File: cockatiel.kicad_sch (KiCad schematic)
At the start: 28 parts

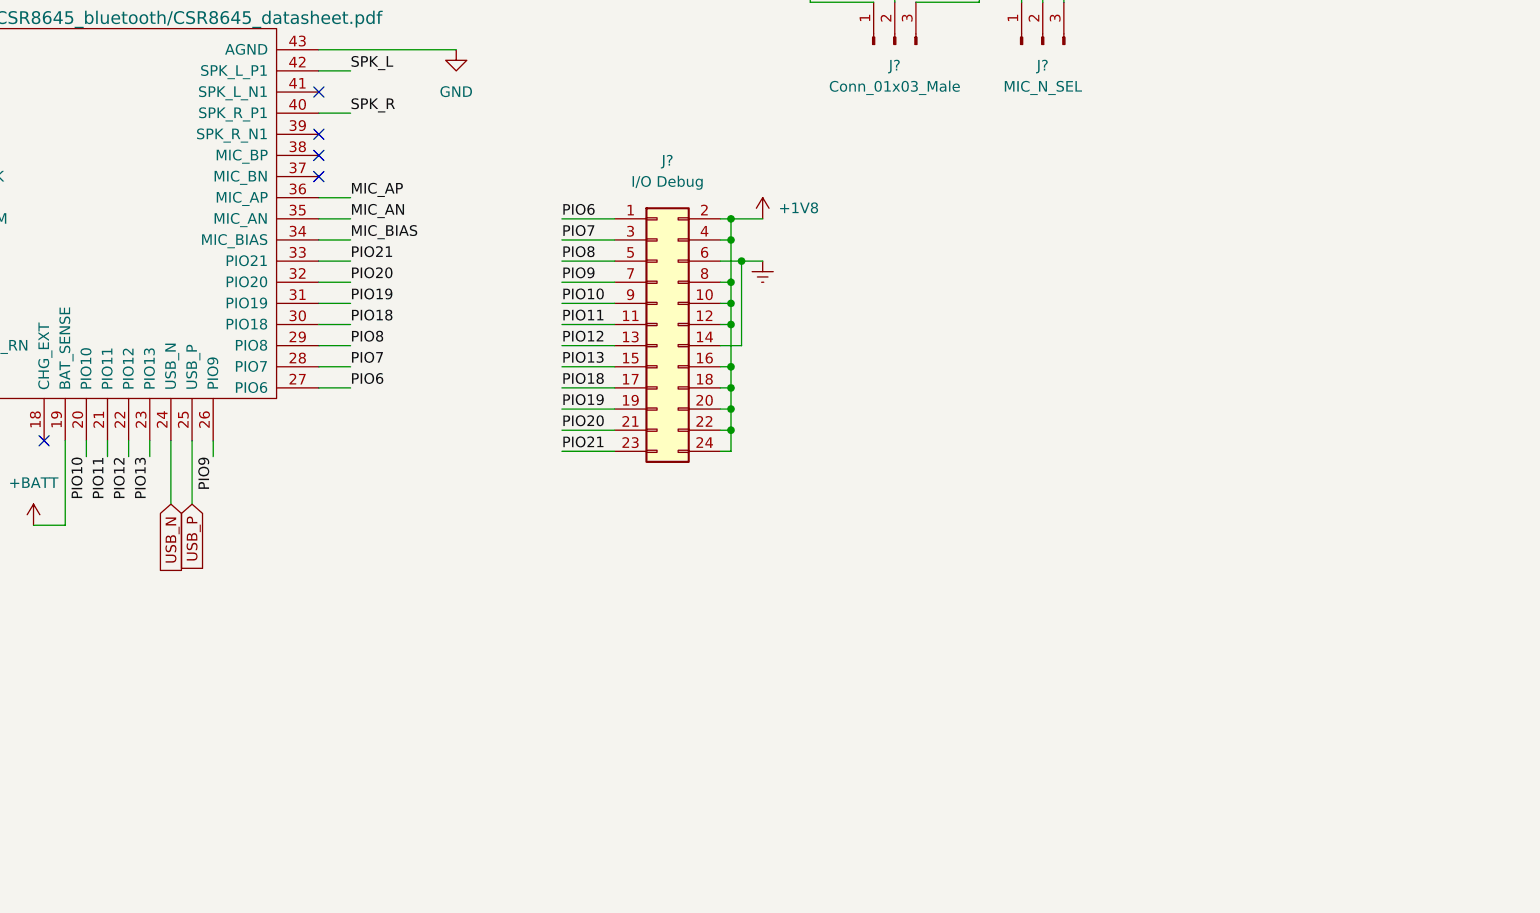
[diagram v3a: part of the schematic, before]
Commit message: Add optional EEPROM
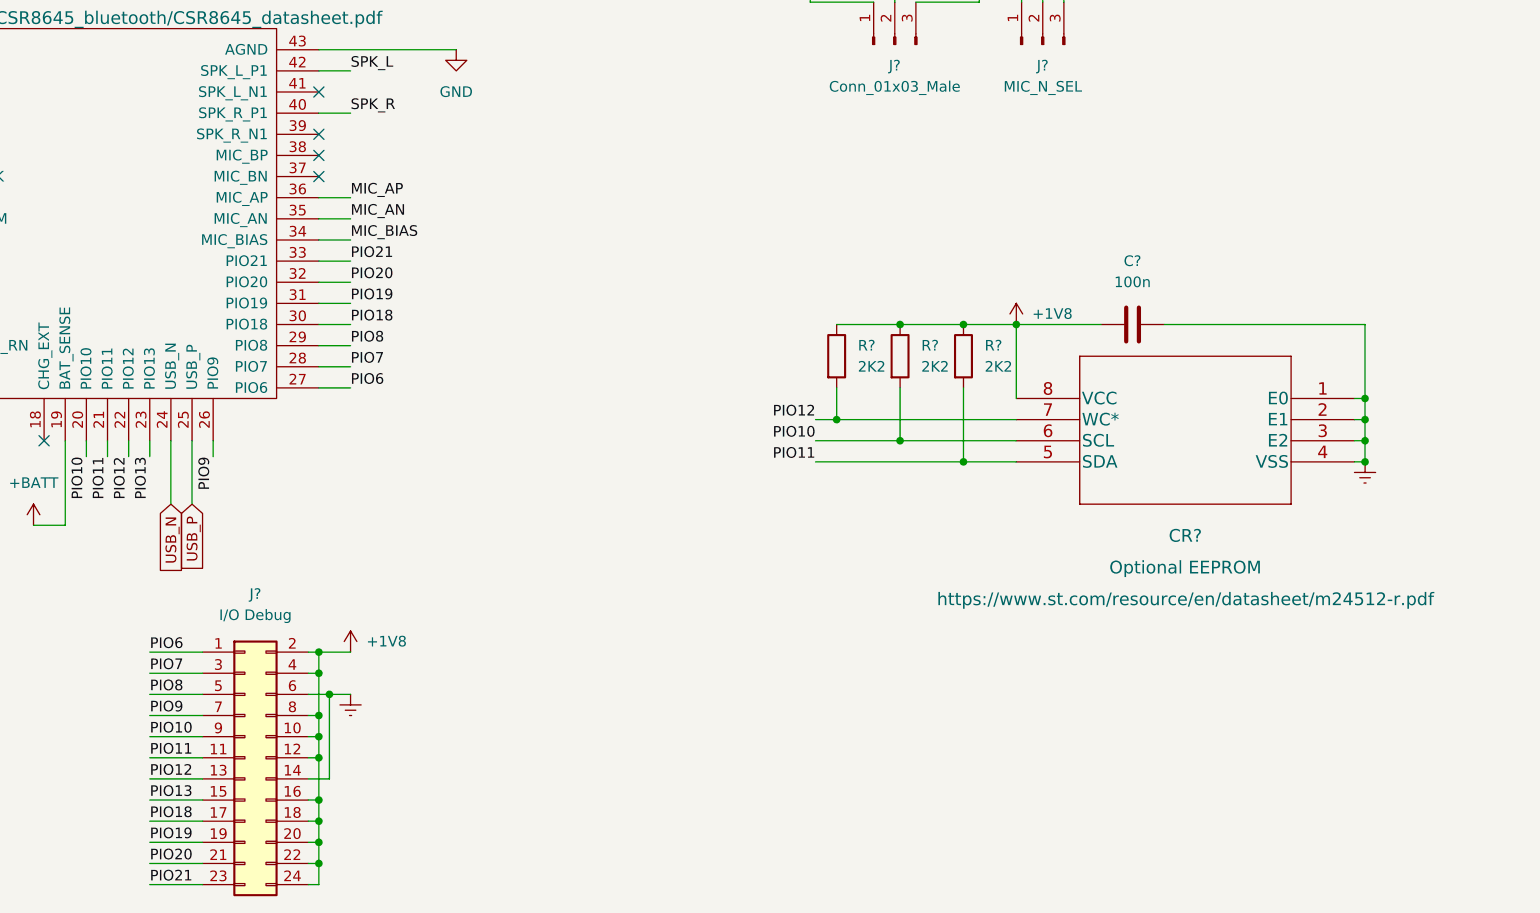
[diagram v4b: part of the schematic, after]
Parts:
- added C?: 100n, Capacitor_SMD:C_0805_2012Metric_Pad1.18x1.45mm_HandSolder, symbol Device:C
- added CR?: Optional EEPROM, st:M24512-RMN6P, symbol 2022-08-27_17-15-02:M24512-RMN6P
- added R? (x3): 2K2, symbol Device:R
- J?: footprint (none) -> Connector_PinHeader_2.54mm:PinHeader_1x04_P2.54mm_Vertical
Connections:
- net +1V8: now also C?.1, CR?.8 (VCC), R?.1, R?.1, R?.1
- net Earth: now also C?.2, CR?.1 (E0), CR?.2 (E1), CR?.3 (E2), CR?.4 (VSS)
- net PIO10: now also CR?.6 (SCL), R?.2
- net PIO11: now also CR?.5 (SDA), R?.2
- net PIO12: now also CR?.7 (WC*), R?.2
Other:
- moved on the sheet: J?

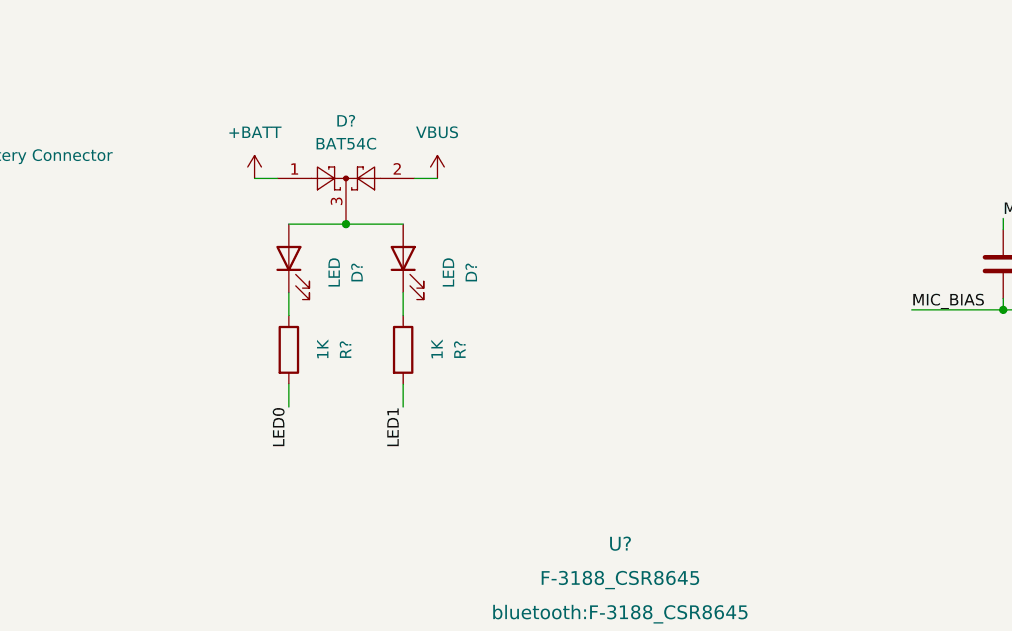
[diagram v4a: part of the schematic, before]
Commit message: Add support for external (panel mount) LEDs
Also correct resistor values to support a set of RGB LEDs.
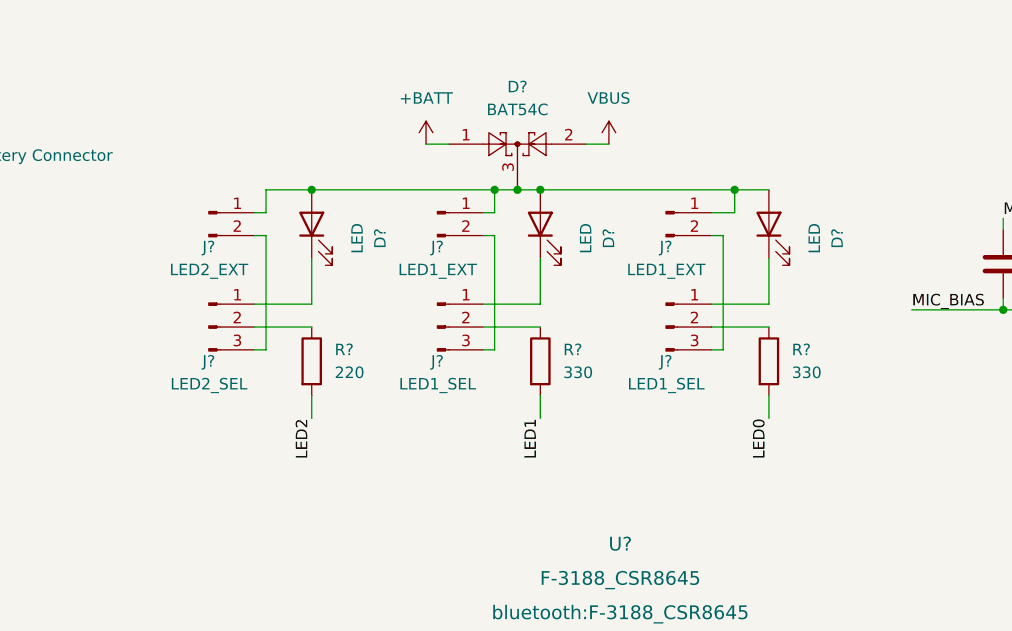
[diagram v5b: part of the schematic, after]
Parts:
- added D?: LED, LED_SMD:LED_0805_2012Metric_Pad1.15x1.40mm_HandSolder, symbol Device:LED
- added J? (x2): LED1_SEL, Connector_PinHeader_2.54mm:PinHeader_1x03_P2.54mm_Vertical, symbol Connector:Conn_01x03_Male
- added J?: LED2_EXT, symbol Connector:Conn_01x02_Male
- added J? (x2): LED1_EXT, Connector_PinHeader_2.54mm:PinHeader_1x02_P2.54mm_Vertical, symbol Connector:Conn_01x02_Male
- added J?: LED2_SEL, Connector_PinHeader_2.54mm:PinHeader_1x03_P2.54mm_Vertical, symbol Connector:Conn_01x03_Male
- added R?: 220, Resistor_SMD:R_0805_2012Metric_Pad1.20x1.40mm_HandSolder, symbol Device:R
- R? (x2): value 1K -> 330
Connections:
- net LED2: now also R?.2
- net at D?.2 (A), D?.2 (A), D?.3: now also D?.2 (A), J?.1 (Pin_1), J?.1 (Pin_1), J?.1 (Pin_1)
- net at D?.1 (K): now also J?.1 (Pin_1); no longer R?.1 (x2)
- new net: J?.2 (Pin_2), R?.1 (x3)
- new net: J?.2 (Pin_2), J?.3 (Pin_3) (x3)
- new net: D?.1 (K), J?.1 (Pin_1)
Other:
- moved on the sheet: D?, R?

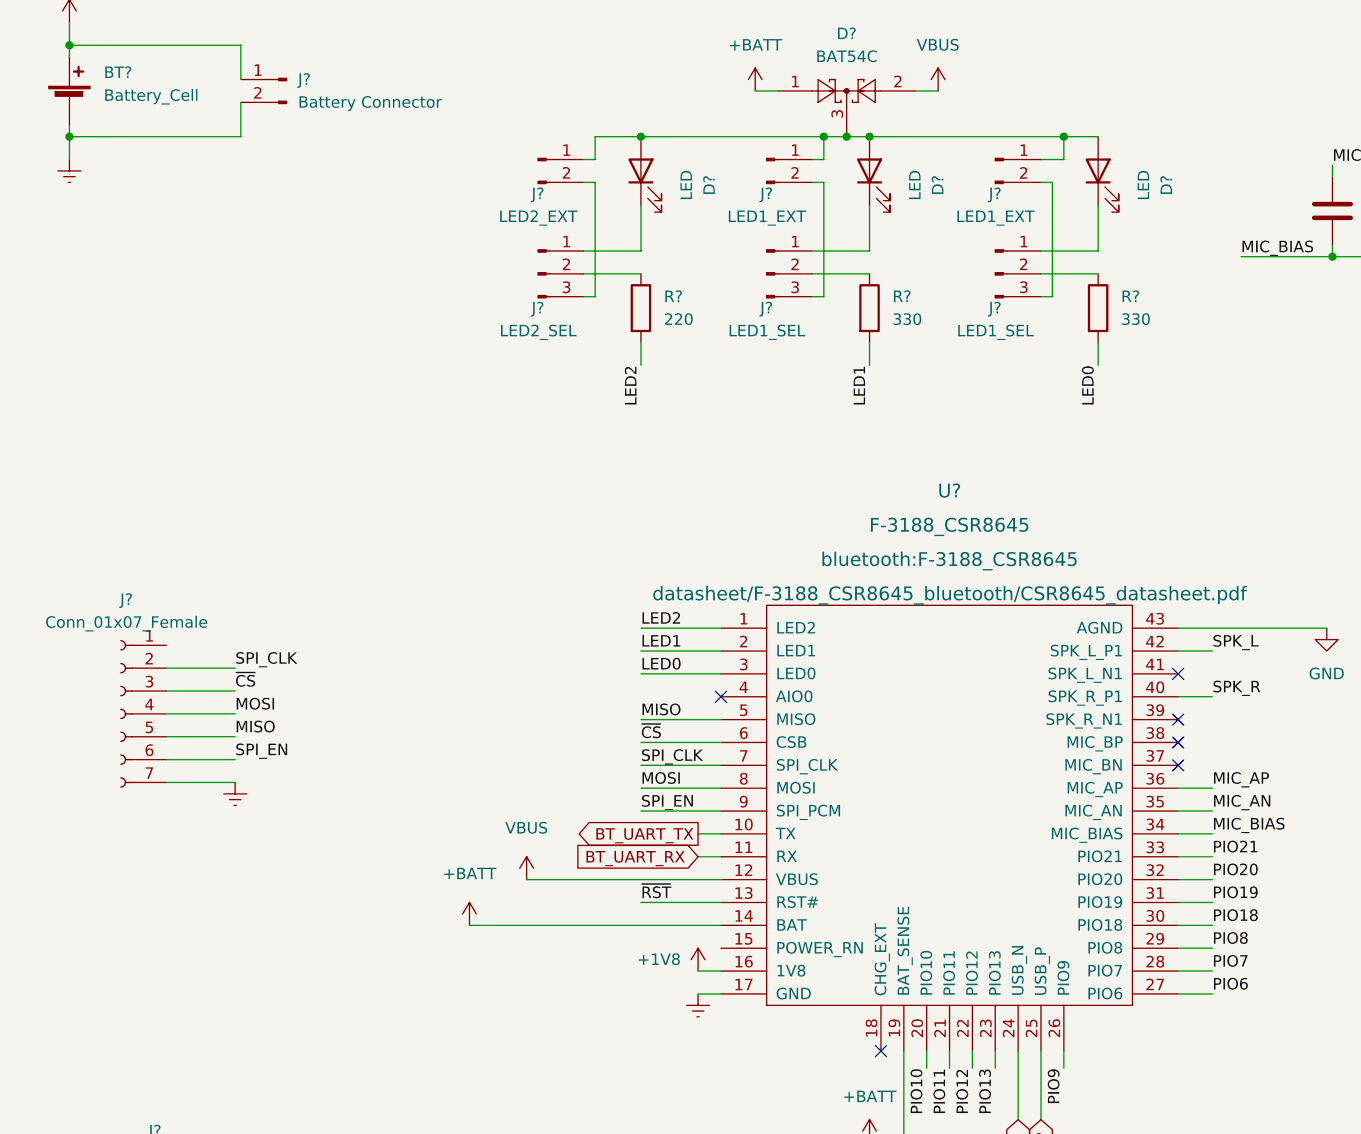
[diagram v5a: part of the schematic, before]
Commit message: Add support for power enable.
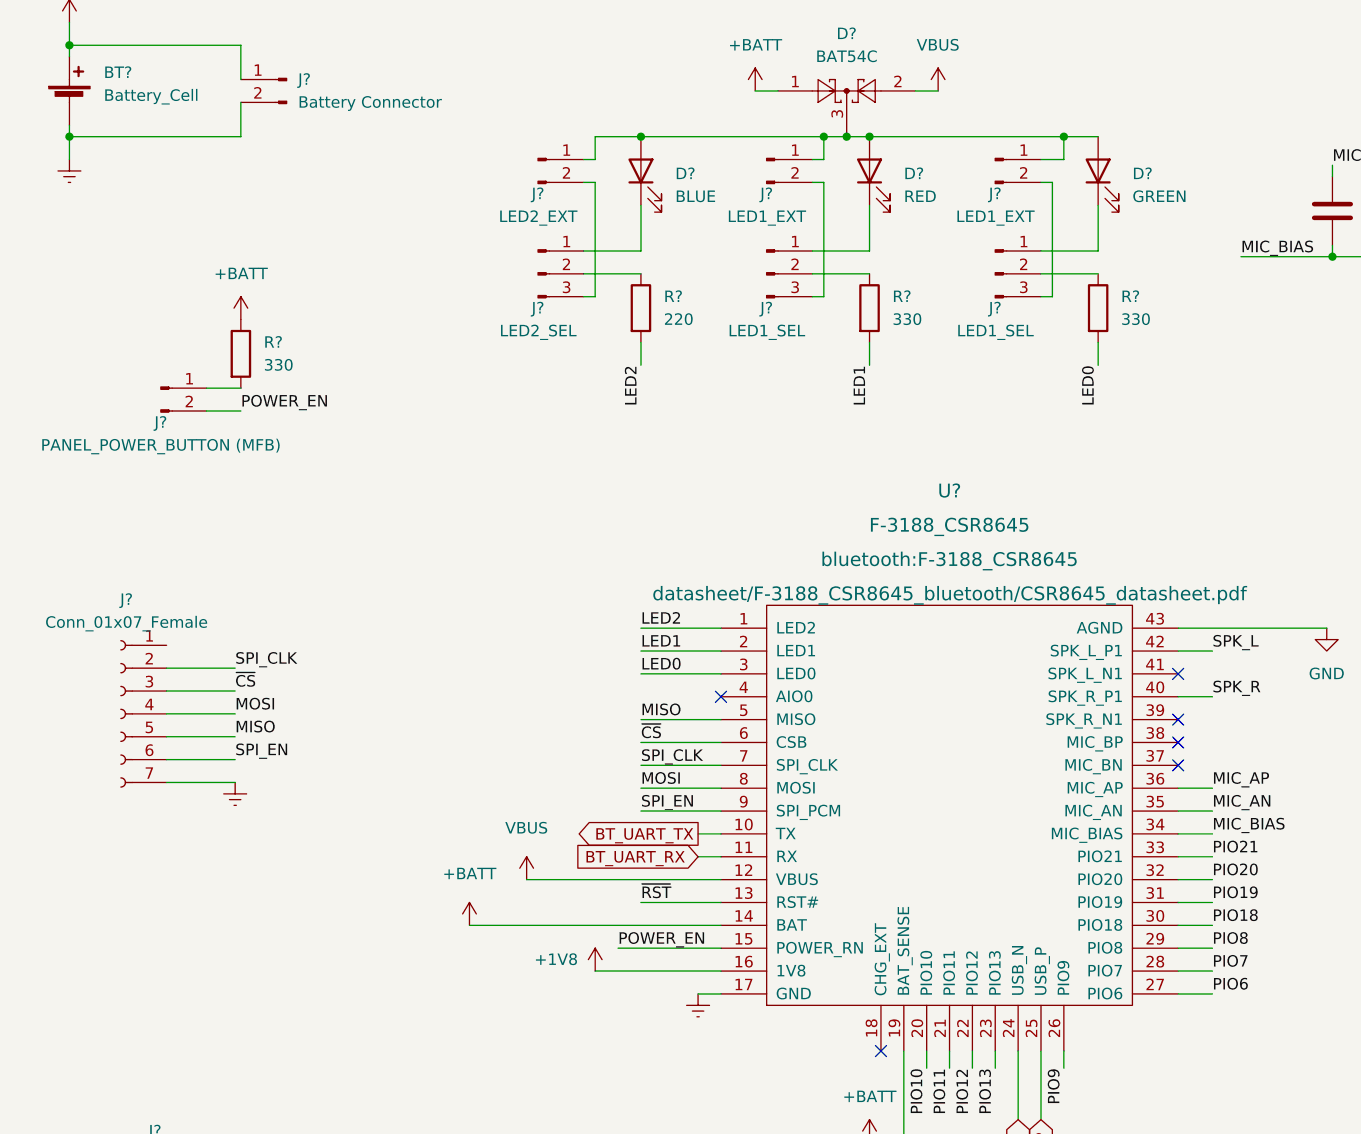
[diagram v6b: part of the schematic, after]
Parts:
- added J?: PANEL_POWER_BUTTON (MFB), Connector_PinHeader_2.54mm:PinHeader_1x02_P2.54mm_Vertical, symbol Connector:Conn_01x02_Male
- added R?: 330, Resistor_SMD:R_0805_2012Metric_Pad1.20x1.40mm_HandSolder, symbol Device:R
- C?, CR?, R? (x3): now left out of the parts list
- D?: value LED -> GREEN
- D?: value LED -> BLUE
- D?: value LED -> RED
- J?: footprint (none) -> Connector_PinHeader_2.54mm:PinHeader_1x02_P2.54mm_Vertical
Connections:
- net +BATT: now also R?.1
- net POWER_EN: now reaches U?.15 (POWER_RN)
- net POWER_EN: now also J?.2 (Pin_2)
- new net: J?.1 (Pin_1), R?.2

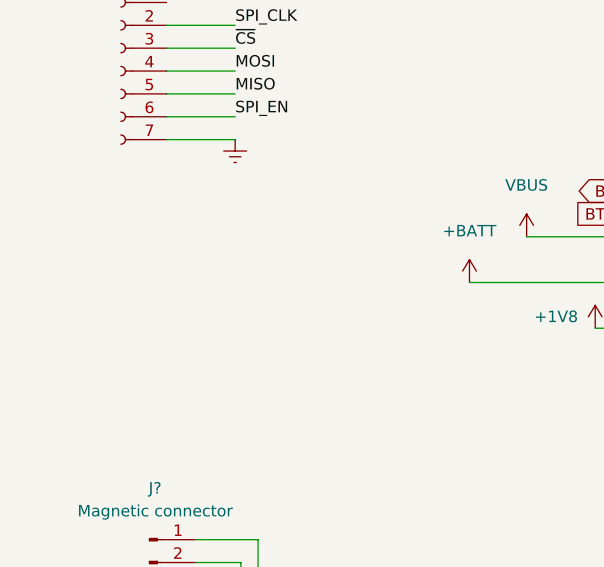
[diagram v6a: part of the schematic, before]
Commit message: Bring out RST# to a pin header
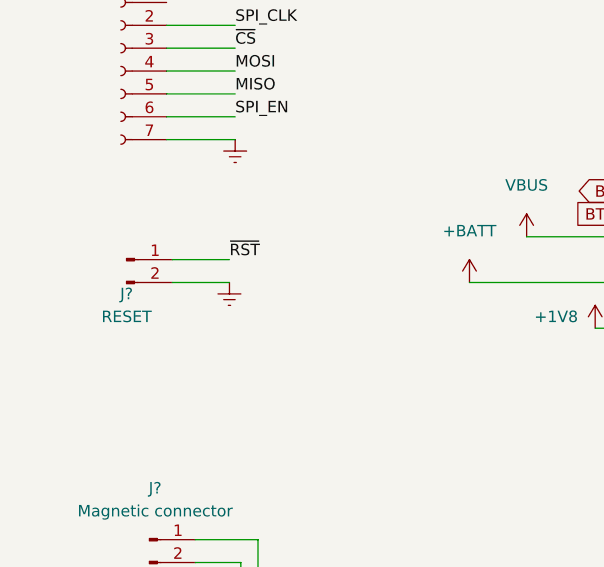
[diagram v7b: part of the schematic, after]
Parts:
- added J?: RESET, Connector_PinHeader_2.54mm:PinHeader_1x02_P2.54mm_Vertical, symbol Connector:Conn_01x02_Male
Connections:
- net Earth: now also J?.2 (Pin_2)
- net ~{RST}: now also J?.1 (Pin_1)
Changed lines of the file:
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@@
+    (stroke (width 0) (type default) (color 0 0 0 0))
+  )
+  (wire (pts (xy 30.48 121.92) (xy 36.83 121.92))
     (stroke (width 0) (type default) (color 0 0 0 0))
   )
@@
   )
   (wire (pts (xy 38.1 153.035) (xy 38.1 175.895))
+    (stroke (width 0) (type default) (color 0 0 0 0))
+  )
+  (wire (pts (xy 30.48 119.38) (xy 36.83 119.38))
     (stroke (width 0) (type default) (color 0 0 0 0))
   )
@@
   )
   (label "PIO8" (at 146.05 124.46 0)
+    (effects (font (size 1.27 1.27)) (justify left bottom))
+  )
+  (label "~{RST}" (at 36.83 119.38 0)
     (effects (font (size 1.27 1.27)) (justify left bottom))
   )
@@
     )
     (property "Datasheet" "~" (id 3) (at 71.12 36.83 0)
+      (effects (font (size 1.27 1.27)) hide)
+    )
+    (pin "1")
+    (pin "2")
+  )
+  (symbol (lib_id "Connector:Conn_01x02_Male") (at 25.4 119.38 0) (unit 1)
+    (in_bom yes) (on_board yes)
+    (property "Reference" "J?" (id 0) (at 25.4 123.19 0))
+    (property "Value" "RESET" (id 1) (at 25.4 125.73 0))
+    (property "Footprint" "Connector_PinHeader_2.54mm:PinHeader_1x02_P2.54mm_Vertical" (id 2) (at 25.4 119.38 0)
+      (effects (font (size 1.27 1.27)) hide)
+    )
+    (property "Datasheet" "~" (id 3) (at 25.4 119.38 0)
       (effects (font (size 1.27 1.27)) hide)
     )
@@
     (pin "9")
   )
+  (symbol (lib_id "power:Earth") (at 36.83 121.92 0) (unit 1)
+    (in_bom yes) (on_board yes) (fields_autoplaced)
+    (property "Reference" "#PWR?" (id 0) (at 36.83 128.27 0)
+      (effects (font (size 1.27 1.27)) hide)
+    )
+    (property "Value" "Earth" (id 1) (at 36.83 125.73 0)
+      (effects (font (size 1.27 1.27)) hide)
+    )
+    (property "Footprint" "" (id 2) (at 36.83 121.92 0)
+      (effects (font (size 1.27 1.27)) hide)
+    )
+    (property "Datasheet" "~" (id 3) (at 36.83 121.92 0)
+      (effects (font (size 1.27 1.27)) hide)
+    )
+    (pin "1")
+  )
   (symbol (lib_id "Device:R") (at 107.95 53.34 0) (unit 1)
     (in_bom yes) (on_board yes) (fields_autoplaced)
@@
       (reference "#PWR?") (unit 1) (value "+1V8") (footprint "")
     )
+    (path "/d13b523b-1509-4495-a088-05de91c0f0b1"
+      (reference "#PWR?") (unit 1) (value "Earth") (footprint "")
+    )
     (path "/def1539a-a57e-4369-be2e-df9d85fff6e6"
       (reference "#PWR?") (unit 1) (value "GND") (footprint "")
@@
       (reference "J?") (unit 1) (value "LED2_EXT") (footprint "Connector_PinHeader_2.54mm:PinHeader_1x02_P2.54mm_Vertical")
     )
+    (path "/48fbcf57-d157-45a3-bb25-2b09bc04196b"
+      (reference "J?") (unit 1) (value "RESET") (footprint "Connector_PinHeader_2.54mm:PinHeader_1x02_P2.54mm_Vertical")
+    )
     (path "/4b4642ab-300c-4f27-8ab8-17e63678d374"
